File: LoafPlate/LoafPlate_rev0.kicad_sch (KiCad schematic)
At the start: 19 parts, among them J1 Ext Connector, J2 Rail Power, J3 Rail Power

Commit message: Rev 0 of the PSUPlate
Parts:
- C2, C3, C5, C6: footprint Capacitor_SMD:C_1206_3216Metric -> Capacitor_SMD:C_0603_1608Metric
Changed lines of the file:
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@@
       (effects (font (size 1.27 1.27)) (justify left))
     )
-    (property "Footprint" "Capacitor_SMD:C_1206_3216Metric" (id 2) (at 58.42 168.91 0)
+    (property "Footprint" "Capacitor_SMD:C_0603_1608Metric" (id 2) (at 58.42 168.91 0)
       (effects (font (size 1.27 1.27)) hide)
     )
@@
       (effects (font (size 1.27 1.27)) (justify left))
     )
-    (property "Footprint" "Capacitor_SMD:C_1206_3216Metric" (id 2) (at 58.42 140.97 0)
+    (property "Footprint" "Capacitor_SMD:C_0603_1608Metric" (id 2) (at 58.42 140.97 0)
       (effects (font (size 1.27 1.27)) hide)
     )
@@
       (effects (font (size 1.27 1.27)) (justify left))
     )
-    (property "Footprint" "Capacitor_SMD:C_1206_3216Metric" (id 2) (at 68.58 140.97 0)
+    (property "Footprint" "Capacitor_SMD:C_0603_1608Metric" (id 2) (at 68.58 140.97 0)
       (effects (font (size 1.27 1.27)) hide)
     )
@@
       (effects (font (size 1.27 1.27)) (justify left))
     )
-    (property "Footprint" "Capacitor_SMD:C_1206_3216Metric" (id 2) (at 68.58 168.91 0)
+    (property "Footprint" "Capacitor_SMD:C_0603_1608Metric" (id 2) (at 68.58 168.91 0)
       (effects (font (size 1.27 1.27)) hide)
     )
@@
     )
     (path "/da31ac0b-2fdb-417e-8753-072db76b611c"
-      (reference "C2") (unit 1) (value "100n") (footprint "Capacitor_SMD:C_1206_3216Metric")
+      (reference "C2") (unit 1) (value "100n") (footprint "Capacitor_SMD:C_0603_1608Metric")
     )
     (path "/be07a1e8-e2e2-43a5-89e5-93eeeb75bc6b"
-      (reference "C3") (unit 1) (value "100n") (footprint "Capacitor_SMD:C_1206_3216Metric")
+      (reference "C3") (unit 1) (value "100n") (footprint "Capacitor_SMD:C_0603_1608Metric")
     )
     (path "/0e0c7124-43b2-4347-b850-8d018f909b22"
@@
     )
     (path "/f1d4bfc4-523d-4478-98dd-64fb48ee012f"
-      (reference "C5") (unit 1) (value "100n") (footprint "Capacitor_SMD:C_1206_3216Metric")
+      (reference "C5") (unit 1) (value "100n") (footprint "Capacitor_SMD:C_0603_1608Metric")
     )
     (path "/f2998a1e-a8a0-4ea5-a4bb-a5b4517d4f69"
-      (reference "C6") (unit 1) (value "100n") (footprint "Capacitor_SMD:C_1206_3216Metric")
+      (reference "C6") (unit 1) (value "100n") (footprint "Capacitor_SMD:C_0603_1608Metric")
     )
     (path "/ac65c696-61af-4334-8ef7-98fcca7cea14"

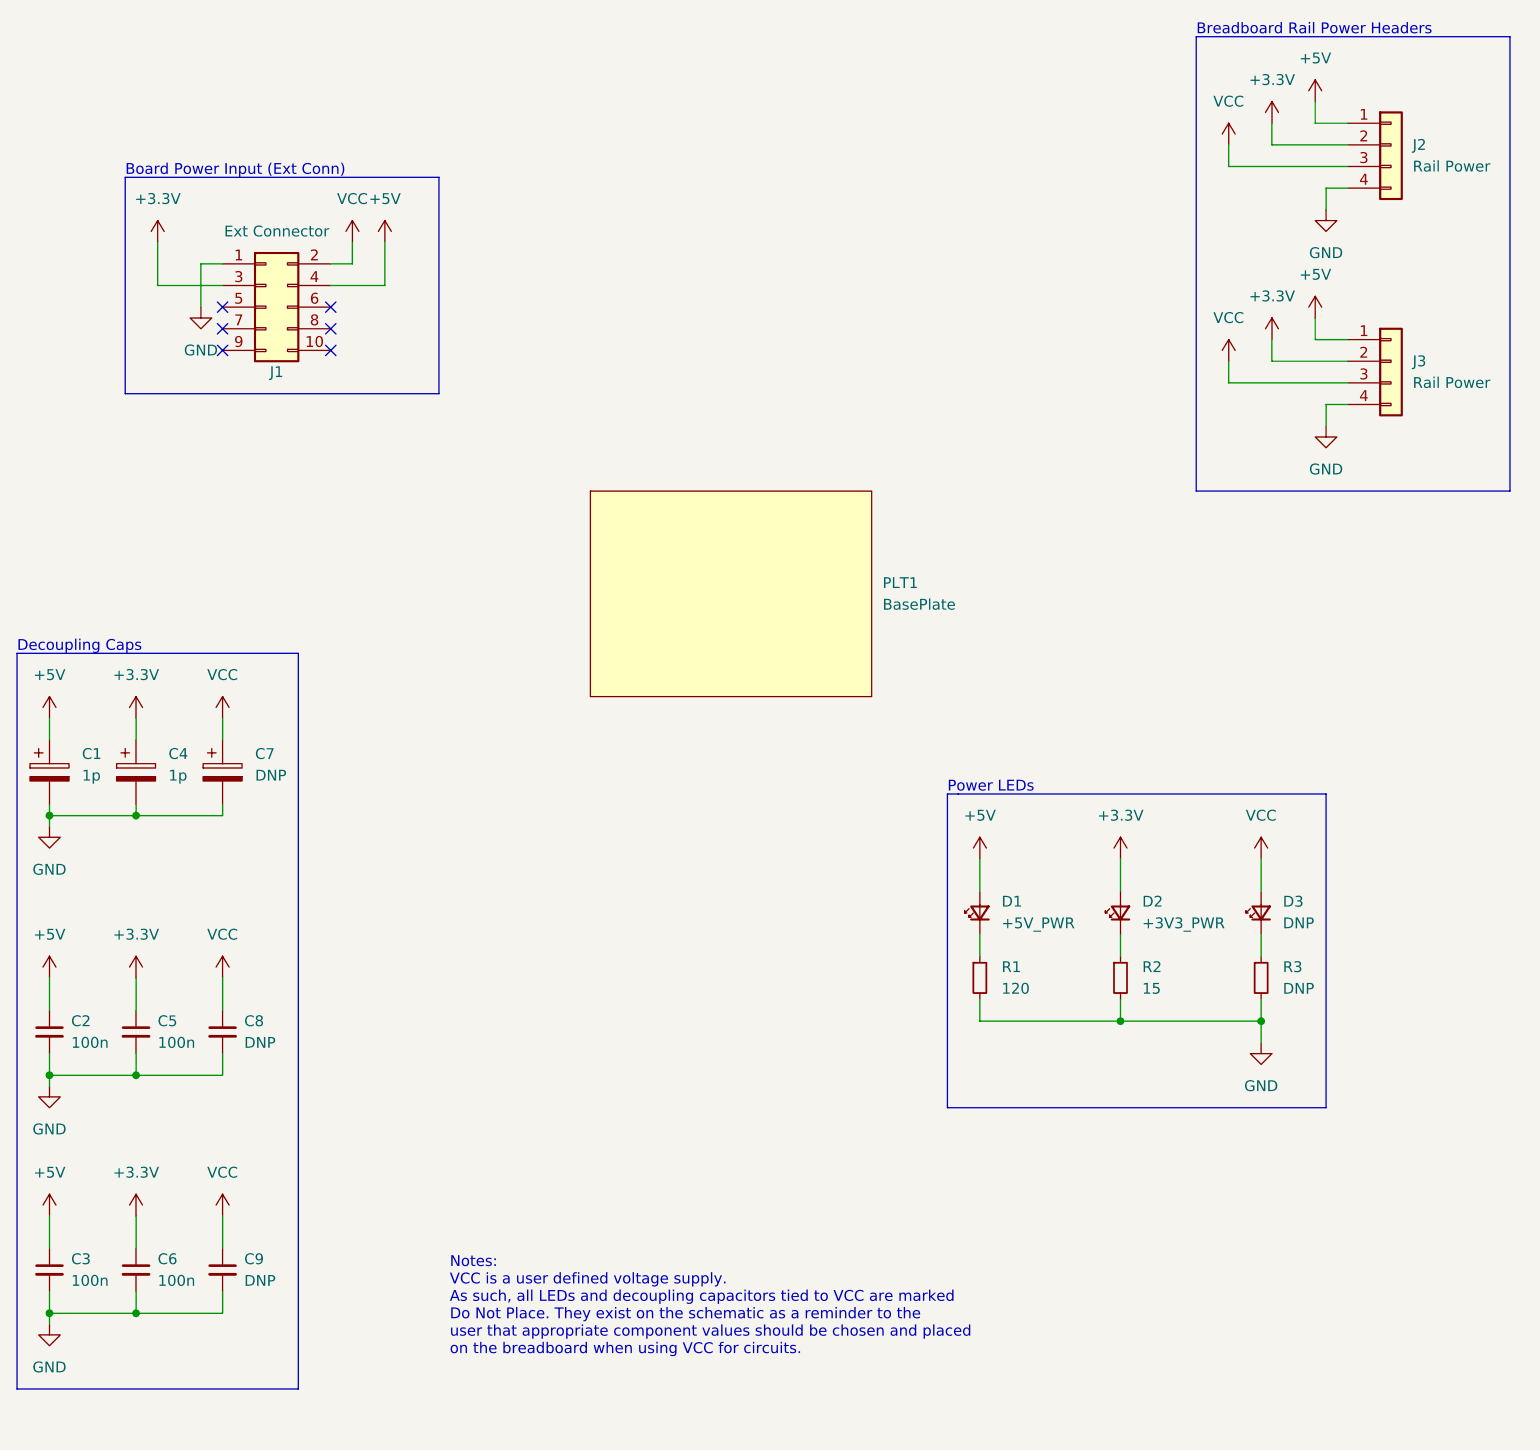
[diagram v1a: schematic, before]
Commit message: Redo layout and routing
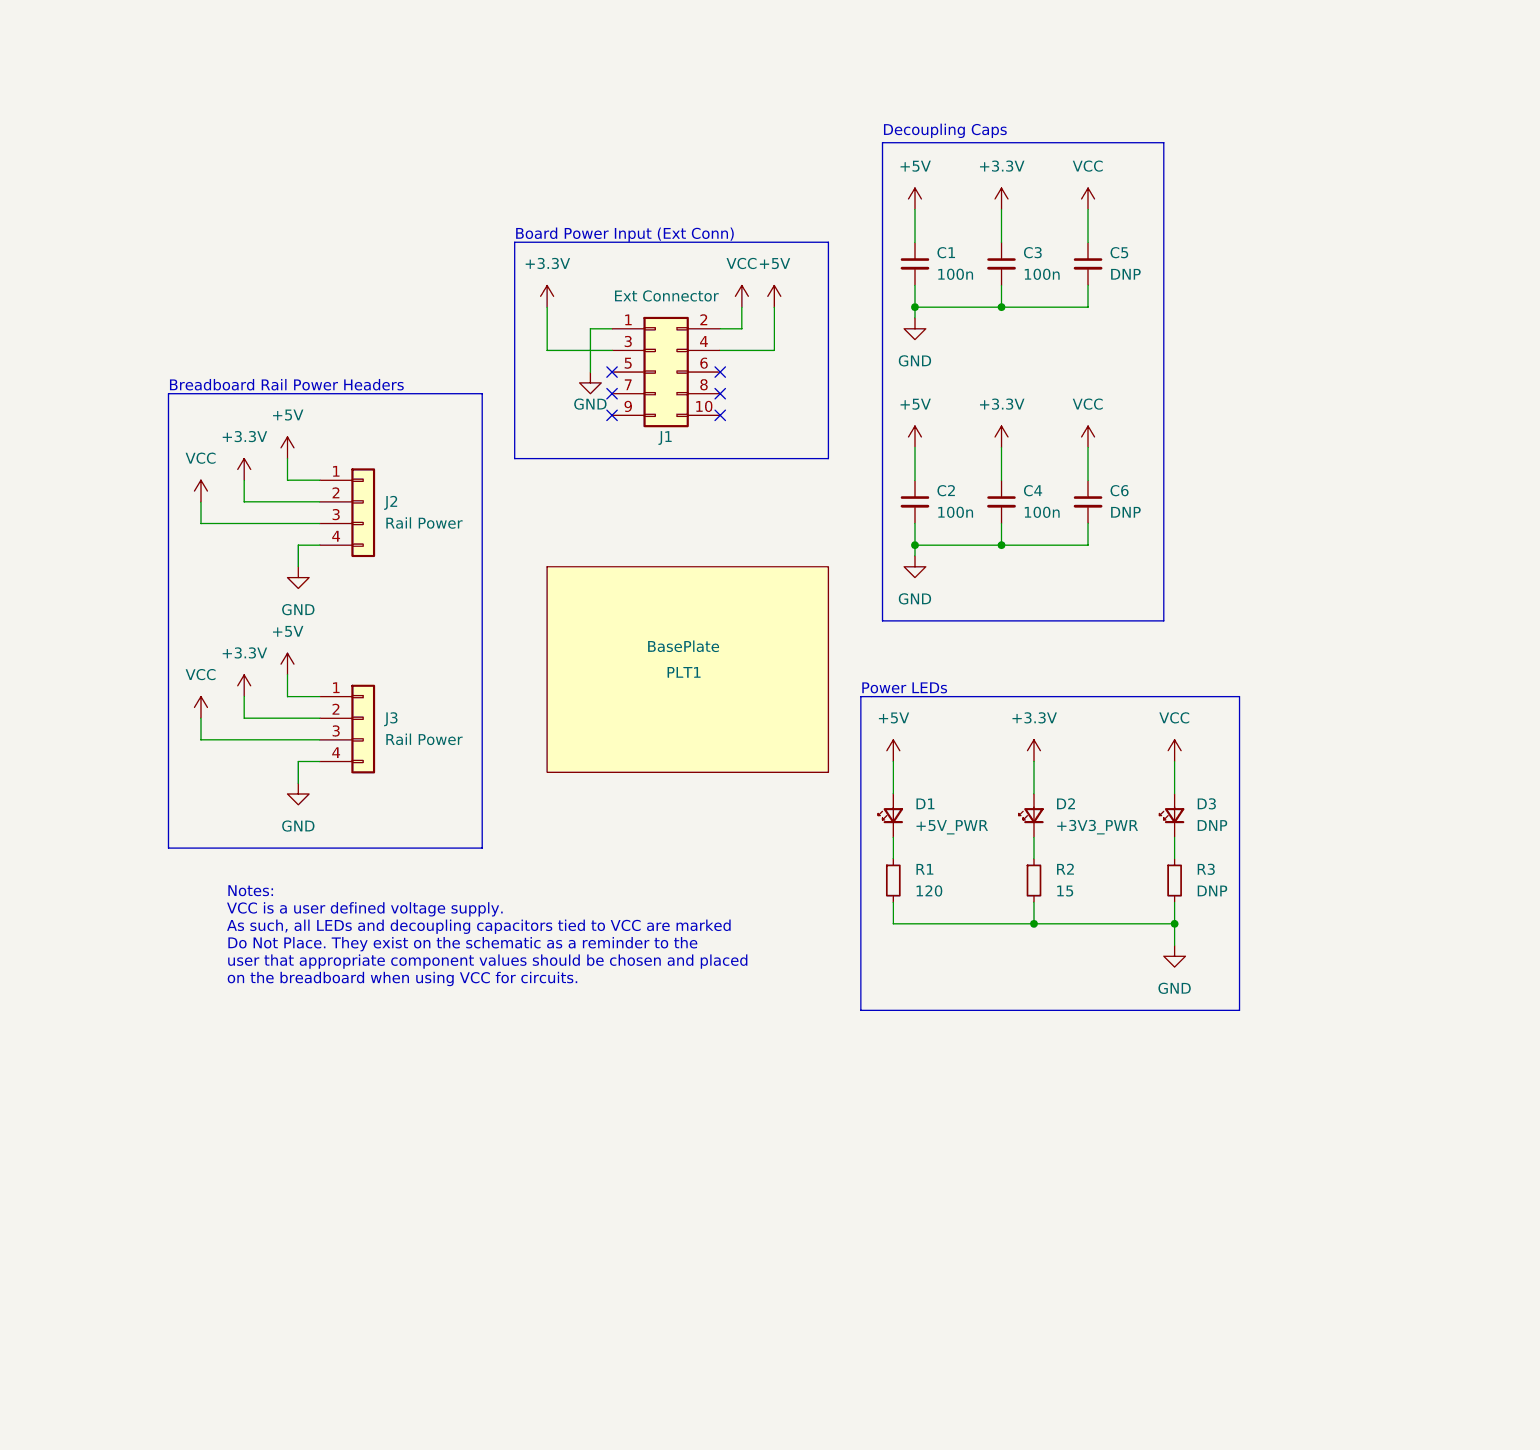
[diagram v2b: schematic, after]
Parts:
- removed C1, C4: 1p, Capacitor_SMD:CP_Elec_3x5.3, symbol Device:C_Polarized
- removed C7: DNP, Capacitor_SMD:CP_Elec_3x5.3, symbol Device:C_Polarized
- renumbered C2 to C1, C3 to C2, C5 to C3, C6 to C4, C8 to C5, C9 to C6
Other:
- moved on the sheet: C1, C2, C3, C4, C5, C6, D1, D2, D3, J1, J2, J3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

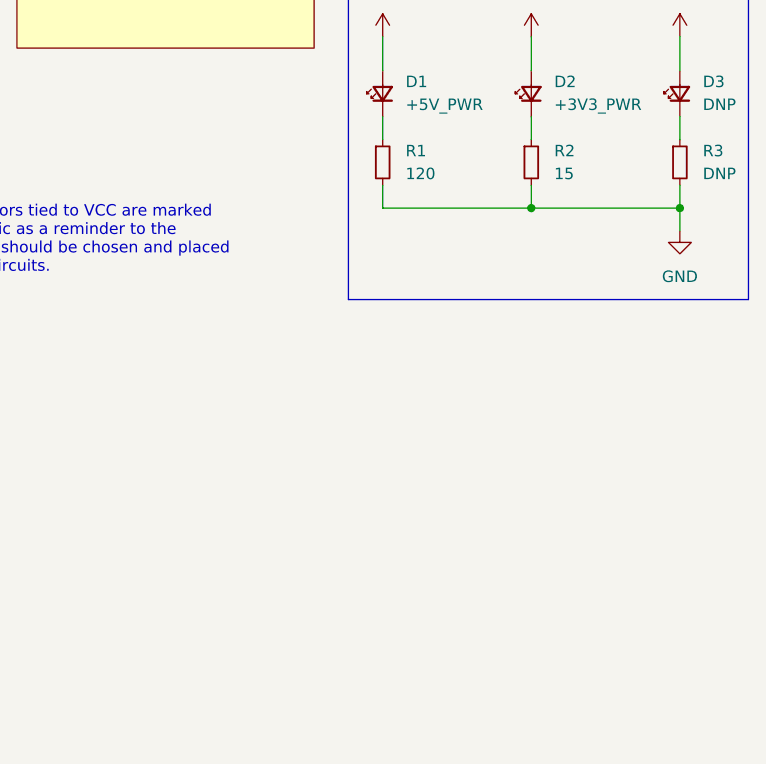
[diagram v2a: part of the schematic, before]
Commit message: Added tooling holes for production.
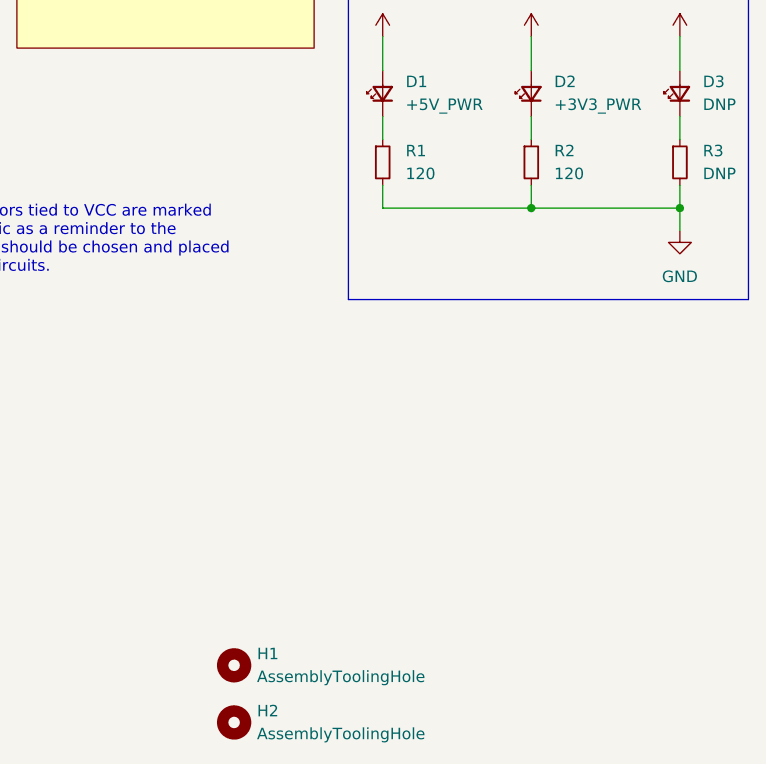
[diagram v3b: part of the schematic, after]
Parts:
- added H1, H2: AssemblyToolingHole, ExtraParts:JLCPCB_ToolingHole, symbol Mechanical:MountingHole
- R2: value 15 -> 120
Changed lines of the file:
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@@
       (effects (font (size 1.27 1.27)) (justify left))
     )
-    (property "Value" "15" (id 1) (at 176.53 124.4599 0)
+    (property "Value" "120" (id 1) (at 176.53 124.4599 0)
       (effects (font (size 1.27 1.27)) (justify left))
     )
@@
     (pin "1")
   )
+  (symbol (lib_id "Mechanical:MountingHole") (at 140.97 179.07 0) (unit 1)
+    (in_bom yes) (on_board yes) (fields_autoplaced)
+    (property "Reference" "H1" (id 0) (at 143.51 177.7999 0)
+      (effects (font (size 1.27 1.27)) (justify left))
+    )
+    (property "Value" "AssemblyToolingHole" (id 1) (at 143.51 180.3399 0)
+      (effects (font (size 1.27 1.27)) (justify left))
+    )
+    (property "Footprint" "ExtraParts:JLCPCB_ToolingHole" (id 2) (at 140.97 179.07 0)
+      (effects (font (size 1.27 1.27)) hide)
+    )
+    (property "Datasheet" "https://jlcpcb.com/help/article/47-How-to-add-tooling-holes-for-PCB-assembly-order" (id 3) (at 140.97 179.07 0)
+      (effects (font (size 1.27 1.27)) hide)
+    )
+  )
   (symbol (lib_id "Device:C_Small") (at 180.34 50.8 0) (unit 1)
     (in_bom no) (on_board no)
@@
     (pin "1")
   )
+  (symbol (lib_id "Mechanical:MountingHole") (at 140.97 185.42 0) (unit 1)
+    (in_bom yes) (on_board yes) (fields_autoplaced)
+    (property "Reference" "H2" (id 0) (at 143.51 184.1499 0)
+      (effects (font (size 1.27 1.27)) (justify left))
+    )
+    (property "Value" "AssemblyToolingHole" (id 1) (at 143.51 186.6899 0)
+      (effects (font (size 1.27 1.27)) (justify left))
+    )
+    (property "Footprint" "ExtraParts:JLCPCB_ToolingHole" (id 2) (at 140.97 185.42 0)
+      (effects (font (size 1.27 1.27)) hide)
+    )
+    (property "Datasheet" "https://jlcpcb.com/help/article/47-How-to-add-tooling-holes-for-PCB-assembly-order" (id 3) (at 140.97 185.42 0)
+      (effects (font (size 1.27 1.27)) hide)
+    )
+  )
   (symbol (lib_id "Connector_Generic:Conn_01x04") (at 95.25 78.74 0) (unit 1)
     (in_bom yes) (on_board yes) (fields_autoplaced)
@@
       (reference "D3") (unit 1) (value "DNP") (footprint "LED_SMD:LED_1206_3216Metric")
     )
+    (path "/6afa7d7b-2499-478b-baf1-06b6a238c071"
+      (reference "H1") (unit 1) (value "AssemblyToolingHole") (footprint "ExtraParts:JLCPCB_ToolingHole")
+    )
+    (path "/7f00d7fe-8f80-4499-a9bb-4f6ebba76e11"
+      (reference "H2") (unit 1) (value "AssemblyToolingHole") (footprint "ExtraParts:JLCPCB_ToolingHole")
+    )
     (path "/21d0e269-33e3-43e9-9de2-28c0e4216b33"
       (reference "J1") (unit 1) (value "Ext Connector") (footprint "Connector_IDC:IDC-Header_2x05_P2.54mm_Horizontal")
@@
     )
     (path "/313964a8-565a-4971-b042-9f580cc0aeb4"
-      (reference "R2") (unit 1) (value "15") (footprint "Resistor_SMD:R_1206_3216Metric")
+      (reference "R2") (unit 1) (value "120") (footprint "Resistor_SMD:R_1206_3216Metric")
     )
     (path "/ebb371da-90b9-4cf1-8881-ed925a4cae39"
